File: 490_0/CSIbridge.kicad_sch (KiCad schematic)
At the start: 1 part, among them J5 5051102291

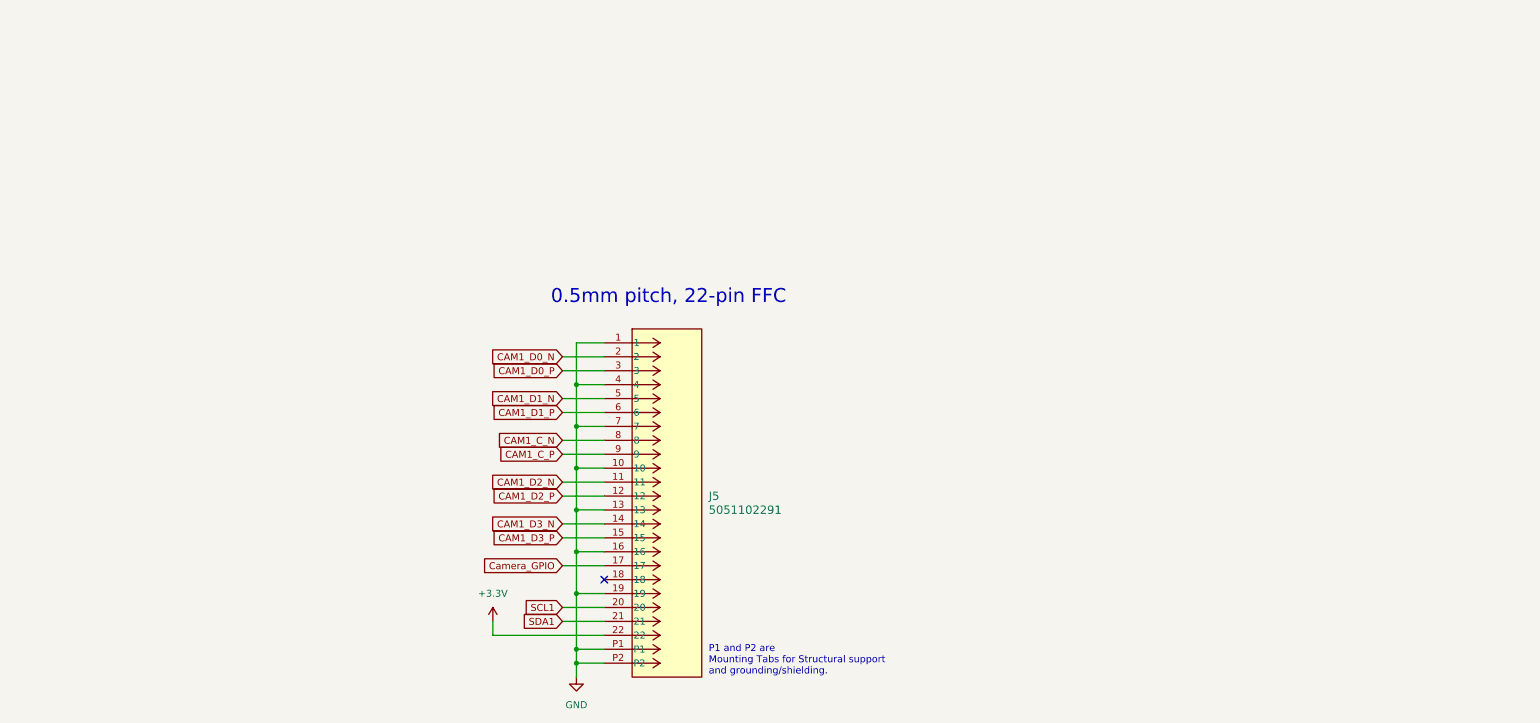
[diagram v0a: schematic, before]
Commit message: Changed PCB block dagram and layout
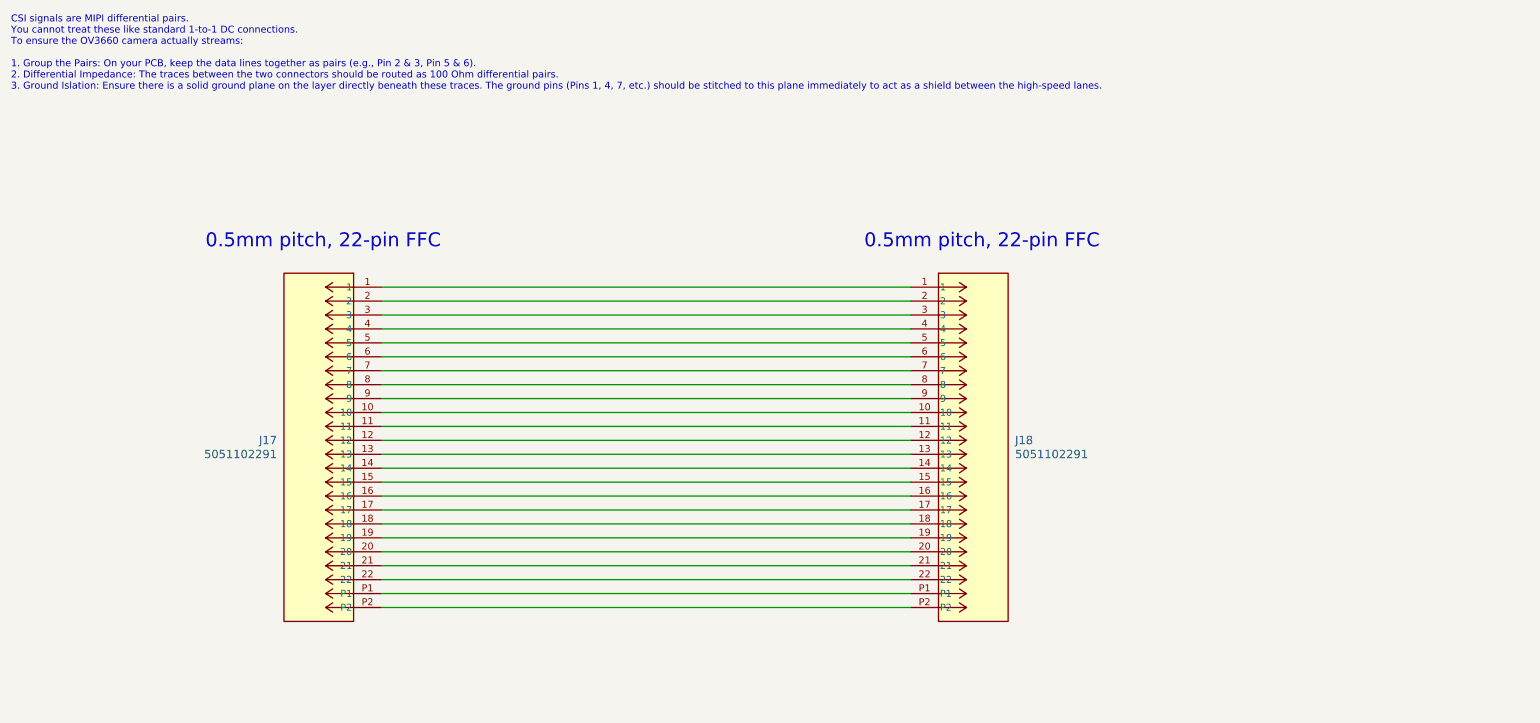
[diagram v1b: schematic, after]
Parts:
- removed J5: 5051102291, CON_5051102291_MOL, symbol capstone_parts:5051102291
- added J17, J18: 5051102291, CON_5051102291_MOL, symbol capstone_parts:5051102291
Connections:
- new net: J17.1, J18.1
- new net: J17.10, J18.10
- new net: J17.11, J18.11
- new net: J17.12, J18.12
- new net: J17.13, J18.13
- new net: J17.14, J18.14
- new net: J17.15, J18.15
- new net: J17.16, J18.16
- new net: J17.17, J18.17
- new net: J17.18, J18.18
- new net: J17.19, J18.19
- new net: J17.2, J18.2
- new net: J17.20, J18.20
- new net: J17.21, J18.21
- new net: J17.22, J18.22
- new net: J17.3, J18.3
- new net: J17.4, J18.4
- new net: J17.5, J18.5
- new net: J17.6, J18.6
- new net: J17.7, J18.7
- new net: J17.8, J18.8
- new net: J17.9, J18.9
- new net: J17.P1, J18.P1
- new net: J17.P2, J18.P2
- no-connect marks 1 -> 0
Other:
- note added: "CSI signals are MIPI differential pairs. You cannot treat these like standard 1-to-1 DC connections. To ensure the OV3660 camera actually streams: 1. Group the Pairs: On your PCB, keep the data lines together as pairs (e.g., Pin 2 & 3, Pin 5 & 6). 2. Differential Impedance: The traces between the two connectors should be routed as 100 Ohm differential pairs. 3. Ground Islation: Ensure there is a 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"
- note removed: "P1 and P2 are Mounting Tabs for Structural support and grounding/shielding."
